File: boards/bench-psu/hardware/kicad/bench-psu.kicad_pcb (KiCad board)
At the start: 4 copper layers, 90 x 76 mm, 116 parts, among them J1 TYPE-C 16PIN 2MD(073), J2 DG301-5.0-04P-14-1000A(H), J3 PZ254V-11-04P, J4 PZ254V-11-05P, Q1 AO4407A, Q11 MMBT3904(RANGE:100-300), Q12 MMBT3904(RANGE:100-300), Q21 MMBT3904(RANGE:100-300), Q22 MMBT3904(RANGE:100-300), SW1 TS-1187A-B-A-B, SW2 TS-1187A-B-A-B, U1 STUSB4500QTR, U11 LMR33630ADDAR, U12 INA226AIDGSR, U2 USBLC6-2SC6, U21 LMR33630ADDAR, U22 INA226AIDGSR, U3 LMR33630ADDAR, U4 AP2112K-3.3TRG1, U5 ESP32-S3-MINI-1-N8, U6 TLV9062IDR

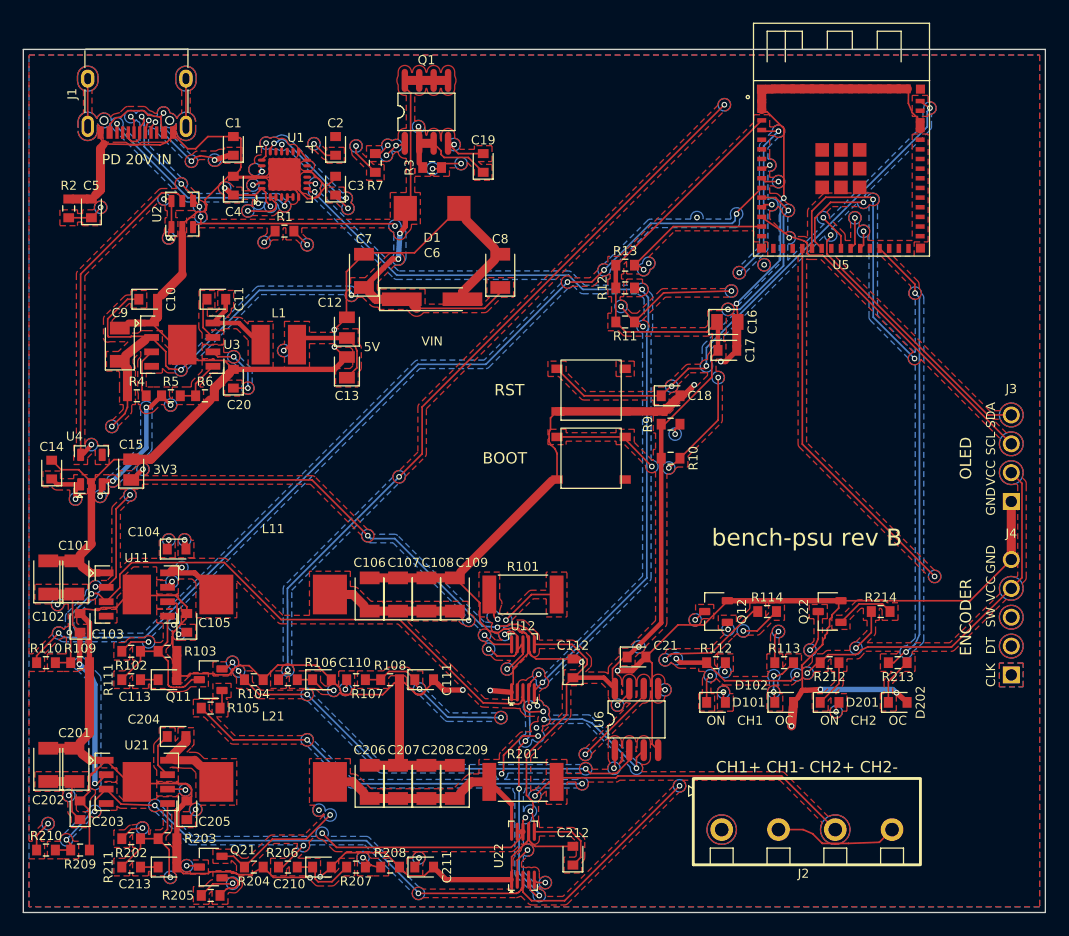
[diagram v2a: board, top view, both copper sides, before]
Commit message: clean up after rev C: hardware/ republished from rev C (stale rev B fab/ removed), sim results and loop plots regenerated from the rev C decks (rev B load-point/switching data dropped), README and sim/README rewritten for rev C (history table, six review rounds, parts bought separately, open point on the loop's mid-band phase)
Co-Authored-By: Claude Opus 5.5 <noreply@anthropic.com>
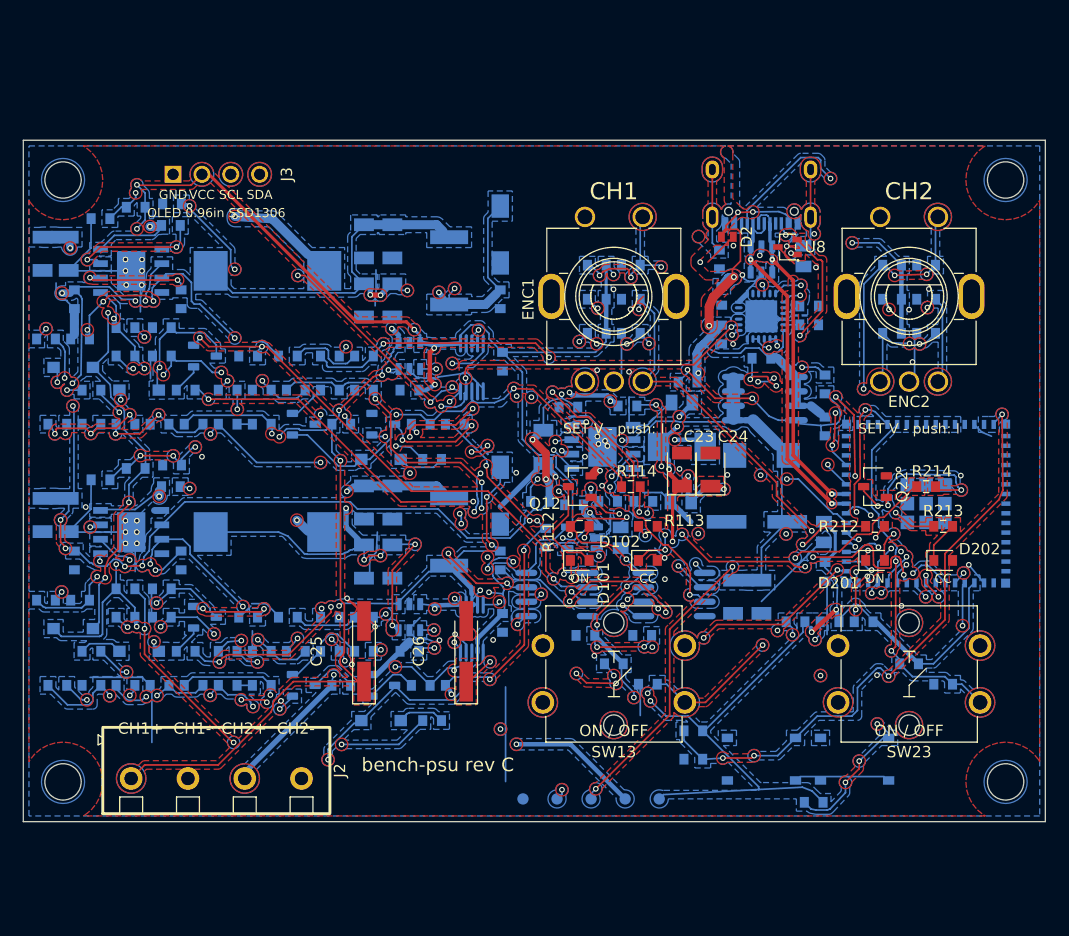
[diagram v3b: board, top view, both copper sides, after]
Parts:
- removed J4: PZ254V-11-05P, tscircuit:PZ254V-11-05P
- added ?: , tscircuit:hole_circle_holeDiameter3.2mm, F.Cu at (141.5, 126.5)
- added ?: , tscircuit:hole_circle_holeDiameter3.2mm, F.Cu at (141.5, 73.5)
- added ?: , tscircuit:hole_circle_holeDiameter3.2mm, F.Cu at (58.5, 126.5)
- added ?: , tscircuit:hole_circle_holeDiameter3.2mm, F.Cu at (58.5, 73.5)
- added C114: 100nF, tscircuit:capacitor_cap0603, B.Cu at (97.0, 84.0)
- added C115: 100nF, tscircuit:capacitor_cap0603, B.Cu at (89.0, 92.0)
- added C116: 100nF, tscircuit:capacitor_cap0603, B.Cu at (85.0, 89.0)
- added C117: 100nF, tscircuit:capacitor_cap0603, B.Cu at (76.0, 95.0)
- added C118: 1uF, tscircuit:capacitor_cap0603, B.Cu at (61.0, 95.0)
- added C119: 100nF, tscircuit:capacitor_cap0603, B.Cu at (67.0, 95.0)
- added C120: 100nF, tscircuit:capacitor_cap0603, B.Cu at (68.1, 75.6)
- added C130: 33nF, tscircuit:capacitor_cap0603, B.Cu at (108.5, 87.0)
- added C131: 33nF, tscircuit:capacitor_cap0603, B.Cu at (108.5, 84.0)
- added C132: 33nF, tscircuit:capacitor_cap0603, B.Cu at (108.5, 81.0)
- added C133: 33nF, tscircuit:capacitor_cap0603, B.Cu at (110.0, 117.9)
- added C214: 100nF, tscircuit:capacitor_cap0603, B.Cu at (97.0, 107.0)
- added C215: 100nF, tscircuit:capacitor_cap0603, B.Cu at (89.0, 115.0)
- added C216: 100nF, tscircuit:capacitor_cap0603, B.Cu at (85.0, 112.0)
- added C217: 100nF, tscircuit:capacitor_cap0603, B.Cu at (76.0, 118.0)
- added C218: 1uF, tscircuit:capacitor_cap0603, B.Cu at (61.0, 118.0)
- added C219: 100nF, tscircuit:capacitor_cap0603, B.Cu at (67.0, 118.0)
- added C22: 100nF, tscircuit:capacitor_cap0603, B.Cu at (109.5, 113.6)
- added C220: 100nF, tscircuit:capacitor_cap0603, B.Cu at (68.1, 98.6)
- added C23: 22uF, tscircuit:capacitor_cap1206, F.Cu at (113.0, 99.0)
- added C230: 33nF, tscircuit:capacitor_cap0603, B.Cu at (134.5, 87.0)
- added C231: 33nF, tscircuit:capacitor_cap0603, B.Cu at (134.5, 84.0)
- added C232: 33nF, tscircuit:capacitor_cap0603, B.Cu at (134.5, 81.0)
- added C233: 33nF, tscircuit:capacitor_cap0603, B.Cu at (136.0, 117.9)
- added C24: 22uF, tscircuit:capacitor_cap1206, F.Cu at (115.5, 99.0)
- added C25: 100uF, tscircuit:RVT1V101M0607_100UF_35V, F.Cu at (85.0, 115.0)
- added C26: 100uF, tscircuit:RVT1V101M0607_100UF_35V, F.Cu at (94.0, 115.0)
- added D13: D, tscircuit:SS54, B.Cu at (97.0, 78.3)
- added D14: D, tscircuit:1N4148W, B.Cu at (65.2, 92.0)
- added D15: D, tscircuit:1N4148W, B.Cu at (86.5, 98.1)
- added D16: D, tscircuit:1N4148W, B.Cu at (59.4, 90.0)
- added D2: ESDA25P35-1U1M, tscircuit:ESDA25P35-1U1M, F.Cu at (117.0, 78.5)
- added D23: D, tscircuit:SS54, B.Cu at (97.0, 101.3)
- added D24: D, tscircuit:1N4148W, B.Cu at (65.2, 115.0)
- added D25: D, tscircuit:1N4148W, B.Cu at (86.5, 121.1)
- added D26: D, tscircuit:1N4148W, B.Cu at (59.4, 113.0)
- added ENC1: EC11E15244B2, tscircuit:EC11E15244B2, F.Cu at (107.0, 84.0)
- added ENC2: EC11E15244B2, tscircuit:EC11E15244B2, F.Cu at (133.0, 84.0)
- added Q13: 2N7002, tscircuit:2N7002, B.Cu at (79.7, 95.0)
- added Q14: MMBT3904(RANGE:100-300), tscircuit:MMBT3904_RANGE_100-300, B.Cu at (86.7, 95.0)
- added Q23: 2N7002, tscircuit:2N7002, B.Cu at (79.7, 118.0)
- added Q24: MMBT3904(RANGE:100-300), tscircuit:MMBT3904_RANGE_100-300, B.Cu at (86.7, 118.0)
- added R115: 10kΩ, tscircuit:resistor_res0603, B.Cu at (82.0, 89.0)
- added R116: 10kΩ, tscircuit:resistor_res0603, B.Cu at (61.0, 92.0)
- added R117: 10kΩ, tscircuit:resistor_res0603, B.Cu at (70.0, 95.0)
- added R118: 330Ω, tscircuit:resistor_res0603, B.Cu at (73.0, 95.0)
- added R119: 10kΩ, tscircuit:resistor_res0603, B.Cu at (58.0, 95.0)
- added R120: 100kΩ, tscircuit:resistor_res0603, B.Cu at (64.0, 95.0)
- added R121: 4.7kΩ, tscircuit:resistor_res0603, B.Cu at (83.0, 95.0)
- added R122: 47kΩ, tscircuit:resistor_res0603, B.Cu at (90.0, 95.0)
- added R123: 47kΩ, tscircuit:resistor_res0603, B.Cu at (93.0, 95.0)
- added R124: 10kΩ, tscircuit:resistor_res0603, B.Cu at (64.9, 75.9)
- added R125: 330Ω, tscircuit:resistor_res0603, B.Cu at (78.3, 89.0)
- added R126: 100kΩ, tscircuit:resistor_res0603, B.Cu at (91.0, 98.1)
- added R130: 3.3kΩ, tscircuit:resistor_res0603, B.Cu at (105.5, 87.0)
- added R131: 3.3kΩ, tscircuit:resistor_res0603, B.Cu at (105.5, 84.0)
- added R132: 3.3kΩ, tscircuit:resistor_res0603, B.Cu at (105.5, 81.0)
- added R133: 3.3kΩ, tscircuit:resistor_res0603, B.Cu at (107.0, 116.1)
- added R215: 10kΩ, tscircuit:resistor_res0603, B.Cu at (82.0, 112.0)
- added R216: 10kΩ, tscircuit:resistor_res0603, B.Cu at (61.0, 115.0)
- added R217: 10kΩ, tscircuit:resistor_res0603, B.Cu at (70.0, 118.0)
- added R218: 330Ω, tscircuit:resistor_res0603, B.Cu at (73.0, 118.0)
- added R219: 10kΩ, tscircuit:resistor_res0603, B.Cu at (58.0, 118.0)
- added R220: 100kΩ, tscircuit:resistor_res0603, B.Cu at (64.0, 118.0)
- added R221: 4.7kΩ, tscircuit:resistor_res0603, B.Cu at (83.0, 118.0)
- added R222: 47kΩ, tscircuit:resistor_res0603, B.Cu at (90.0, 118.0)
- added R223: 47kΩ, tscircuit:resistor_res0603, B.Cu at (93.0, 118.0)
- added R224: 10kΩ, tscircuit:resistor_res0603, B.Cu at (64.9, 98.9)
- added R225: 330Ω, tscircuit:resistor_res0603, B.Cu at (78.3, 112.0)
- added R226: 100kΩ, tscircuit:resistor_res0603, B.Cu at (91.0, 121.1)
- added R230: 3.3kΩ, tscircuit:resistor_res0603, B.Cu at (131.5, 87.0)
- added R231: 3.3kΩ, tscircuit:resistor_res0603, B.Cu at (131.5, 84.0)
- added R232: 3.3kΩ, tscircuit:resistor_res0603, B.Cu at (131.5, 81.0)
- added R233: 3.3kΩ, tscircuit:resistor_res0603, B.Cu at (133.0, 116.1)
- added SW13: B3F-4055, tscircuit:B3F-4055, F.Cu at (107.0, 117.0)
- added SW23: B3F-4055, tscircuit:B3F-4055, F.Cu at (133.0, 117.0)
- added TH11: 10kΩ, tscircuit:NCP18XH103F03RB, B.Cu at (61.8, 76.9)
- added TH21: 10kΩ, tscircuit:NCP18XH103F03RB, B.Cu at (61.8, 99.9)
- added TP1: test_point_smtpad_circle_d1, tscircuit:test_point_smtpad_circle_d1, B.Cu at (102.0, 128.0)
- added TP2: test_point_smtpad_circle_d1, tscircuit:test_point_smtpad_circle_d1, B.Cu at (105.0, 128.0)
- added TP3: test_point_smtpad_circle_d1, tscircuit:test_point_smtpad_circle_d1, B.Cu at (108.0, 128.0)
- added TP4: test_point_smtpad_circle_d1, tscircuit:test_point_smtpad_circle_d1, B.Cu at (111.0, 128.0)
- added TP5: test_point_smtpad_circle_d1, tscircuit:test_point_smtpad_circle_d1, B.Cu at (99.0, 128.0)
- added U13: INA181A2IDBVR, tscircuit:INA181A2IDBVR, B.Cu at (89.0, 89.0)
- added U23: INA181A2IDBVR, tscircuit:INA181A2IDBVR, B.Cu at (89.0, 112.0)
- added U7: TLV9062IDR, tscircuit:TLV9062IDR, B.Cu at (112.3, 110.0)
- added U8: ESDA25W, tscircuit:ESDA25W, F.Cu at (122.3, 79.4)
- C1, C101, C102, C104, C105, C106, C107, C108, C109, C11, C110, C111, C112, C113, C12, C13, C14, C15, C16, C17, C18, C19, C2, C20, C201, C202, C204, C205, C206, C207, C208, C209, C21, C210, C211, C212, C213, C3, C4, C6, C7, C8, C9, D1, J1, Q1, Q11, Q21, R1, R10, R101, R102, R103, R105, R106, R107, R108, R109, R11, R110, R111, R12, R13, R2, R201, R202, R203, R205, R206, R207, R208, R209, R210, R211, R3, R4, R5, R6, R7, R9, SW1, SW2, U1, U11, U12, U2, U21, U22, U3, U4, U5, U6: moved to B.Cu
- C10, C103, C203: value 100nF -> 220nF; moved to B.Cu
- C5: footprint tscircuit:capacitor_cap0603 -> tscircuit:capacitor_cap0805; moved to B.Cu
- L1: value 15µH -> 6.8µH; footprint tscircuit:SWPA4030S150MT -> tscircuit:FXL0530-6R8-M; moved to B.Cu
- L11, L21: value 10µH -> 15µH; footprint tscircuit:FXL1040-100-M -> tscircuit:FXL1040-150-M; moved to B.Cu
- R104, R204: value 2.4kΩ -> 2.2kΩ; moved to B.Cu
- moved J3 74.3 mm to (72.0, 73.0), turned to 0 degrees
- moved C5 62.8 mm to (123.7, 80.2)
- moved R2 57.5 mm to (116.3, 80.5)
- moved J1 55.6 mm to (120.0, 74.8)
- moved J2 52.2 mm to (72.0, 126.2)
- moved U2 51.2 mm to (120.0, 80.5)
- moved C1 45.0 mm to (116.5, 83.7)
- moved C4 45.0 mm to (116.5, 87.1)
- moved R7 44.1 mm to (125.6, 91.5)
- moved C2 44.0 mm to (124.2, 84.6), turned to 180 degrees
- moved C14 43.9 mm to (101.0, 105.0)
- moved U1 43.8 mm to (120.0, 85.5)
- moved U4 43.6 mm to (104.2, 105.0), turned to 90 degrees
- moved C15 43.5 mm to (107.6, 105.0)
- moved R1 43.5 mm to (120.0, 89.2)
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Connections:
- net ISET1_DRV renamed ISINK1_DRV
- net ISET1_E renamed ISINK1_E
- net ISET2_DRV renamed ISINK2_DRV
- net ISET2_E renamed ISINK2_E
- net LED_OC1 renamed LED_CC1
- net LED_OC2 renamed LED_CC2
- net Net-(R111-Pad2) renamed LAG1
- net Net-(R211-Pad2) renamed LAG2
- U2 pad 1: USB_DN -> USB_DP
- U2 pad 3: USB_DP -> USB_DN
- U2 pad 4: USB_DP -> USB_DN
- U2 pad 6: USB_DN -> USB_DP
- U5 pad 15: (no net) -> ISET1
- U5 pad 16: (no net) -> ISET2
- U5 pad 17: (no net) -> ENC2_A
- U5 pad 18: (no net) -> ENC2_B
- U5 pad 19: ENC_A -> ENC1_A
- U5 pad 20: ENC_B -> ENC1_B
- U5 pad 21: ENC_SW -> ENC1_SW
- U5 pad 22: (no net) -> ENC2_SW
- U5 pad 34: (no net) -> BTN1
- U5 pad 35: (no net) -> BTN2
- U5 pad 5: (no net) -> NTC1
- U5 pad 6: (no net) -> NTC2
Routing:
- net GND: track 415.6 -> 162.5 mm, vias 15 -> 51
- net NTC1: track 0.00 -> 92.6 mm, vias 0 -> 6
- net NTC2: track 0.00 -> 79.8 mm, vias 0 -> 6
- net ISET1: track 0.00 -> 79.4 mm, vias 0 -> 5
- net ISET2: track 0.00 -> 74.7 mm, vias 0 -> 5
- net V3V3: track 219.9 -> 288.4 mm, vias 10 -> 27
- net CC1_OUT: track 0.00 -> 59.2 mm, vias 0 -> 4
- net V5: track 35.1 -> 92.3 mm, vias 6 -> 17
- net CC2_OUT: track 0.00 -> 54.0 mm, vias 0 -> 4
- net ENC_B: track 53.3 -> 0.00 mm, vias 2 -> 0
- net CC1_NEG: track 0.00 -> 50.8 mm, vias 0 -> 3
- net USB_DP: track 77.8 -> 28.1 mm, vias 8 -> 2
- net ENC_SW: track 49.5 -> 0.00 mm, vias 1 -> 0
- net ISENS1_F: track 0.00 -> 49.0 mm, vias 0 -> 4
- net USB_DN: track 77.2 -> 29.2 mm, vias 6 -> 2
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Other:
- board size 90 x 76 mm -> 90 x 60 mm
- board text added: "CC"
- board text added: "OLED 0.96in SSD1306"
- board text added: "ON / OFF"
- board text added: "SET V - push: I"
- board text added: "V5"
- board text added: "VBUS"
- board text added: "bench-psu rev C"
- board text added: "bench-psu rev C - USB-C PD 20 V in"
- board text removed: "5V"
- board text removed: "CH1 / CH2: 1.6-16.6 V, 3 A, hardware OC trip"
- board text removed: "CLK"
- board text removed: "DT"
- board text removed: "ENCODER"
- board text removed: "I2C IO8/IO9: INA226 0x40 / 0x41, STUSB4500 0x28, OLED 0x3C"
- board text removed: "OC"
- board text removed: "OLED"
- board text removed: "PD 20V IN"
- board text removed: "PWM IO4/IO5 EN IO6/IO7 OC LED IO21/IO47 ENC IO15/16/17"
- board text removed: "SW"
- board text removed: "bench-psu rev B"
- board text removed: "bench-psu rev B - USB-C PD 20 V in"

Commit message: hardware/ republished: USB pair vias 0.3 mm drill (standard price class; VibePCB widen_thin_vias + 0.3 mm via rule)
Co-Authored-By: Claude Opus 5.5 <noreply@anthropic.com>
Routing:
- net GND: track 162.5 -> 509.4 mm, vias 51 -> 41
